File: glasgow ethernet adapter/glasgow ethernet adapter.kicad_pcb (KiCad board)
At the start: 2 copper layers, 33 parts, among them J1 Glasgow Port, J2 RJ45_Amphenol_RJMG1BD3B8K1ANR, U1 MxL86110

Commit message: WIP
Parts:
- added C17: 4.7u, Capacitor_SMD:C_1206_3216Metric, F.Cu at (178.2, 121.3)
- added C18: 0.1u, Capacitor_SMD:C_0402_1005Metric, F.Cu at (198.8, 100.2)
- added C19: 0.1u, Capacitor_SMD:C_0402_1005Metric, F.Cu at (162.1, 95.9)
- added C20: 4.7u, Capacitor_SMD:C_1206_3216Metric, F.Cu at (150.0, 82.5)
- added C21: 0.1u, Capacitor_SMD:C_0402_1005Metric, F.Cu at (198.9, 101.7)
- added C22: 0.1u, Capacitor_SMD:C_0402_1005Metric, F.Cu at (139.6, 110.4)
- added D1: LED, Diode_SMD:D_0603_1608Metric, F.Cu at (135.7, 87.3)
- added D2: LED, Diode_SMD:D_0603_1608Metric, F.Cu at (135.7, 84.2)
- added D3: LED, Diode_SMD:D_0603_1608Metric, F.Cu at (135.7, 81.1)
- added R14: 49.9, Resistor_SMD:R_0402_1005Metric, F.Cu at (155.4, 98.9)
- added R15: 49.9, Resistor_SMD:R_0402_1005Metric, F.Cu at (155.4, 101.7)
- added R16: 49.9, Resistor_SMD:R_0402_1005Metric, F.Cu at (155.4, 103.6)
- added R17: R, Resistor_SMD:R_0402_1005Metric, F.Cu at (138.1, 87.3)
- added R18: R, Resistor_SMD:R_0402_1005Metric, F.Cu at (138.1, 84.2)
- added R19: R, Resistor_SMD:R_0402_1005Metric, F.Cu at (138.1, 81.1)
- C1, C2: value C -> 12p; footprint Capacitor_SMD:C_0603_1608Metric -> Capacitor_SMD:C_0402_1005Metric
- C10, C3, C4, C5, C6, C7, C8, C9: value C -> 0.1u; footprint Capacitor_SMD:C_0603_1608Metric -> Capacitor_SMD:C_0402_1005Metric
- J2: value RJ45_Amphenol_RJMG1BD3B8K1ANR -> RJ45_Amphenol_RJMG1S8008101BR; footprint Connector_RJ:RJ45_Amphenol_RJMG1BD3B8K1ANR -> glasgow:AMPHENOL_RJMG1S8008101BR
- R1, R2, R3, R4, R6, R7, R8, R9: value R -> R-3-way; footprint Resistor_SMD:R_0603_1608Metric -> glasgow:R-3-Way_0402_1005Metric
- R10: value 49.9 -> 0; footprint Resistor_SMD:R_0603_1608Metric -> Resistor_SMD:R_0402_1005Metric
- R11: value 49.9 -> R; footprint Resistor_SMD:R_0603_1608Metric -> Resistor_SMD:R_0402_1005Metric
- R12: value 49.9 -> 2.49K; footprint Resistor_SMD:R_0603_1608Metric -> Resistor_SMD:R_0402_1005Metric
- R13: footprint Resistor_SMD:R_0603_1608Metric -> Resistor_SMD:R_0402_1005Metric
- R5: value 2.49K -> R-3-way; footprint Resistor_SMD:R_0603_1608Metric -> glasgow:R-3-Way_0402_1005Metric
- U1: footprint Package_DFN_QFN:QFN-40-1EP_5x5mm_P0.4mm_EP3.8x3.8mm -> glasgow:QFN-40-1EP_5x5mm_P0.4mm_EP3.8x3.8mm
- moved R6 61.7 mm to (153.4, 89.4), turned to 90 degrees
- moved C14 59.9 mm to (153.4, 104.2)
- moved R3 59.8 mm to (155.1, 88.8), turned to 90 degrees
- moved C13 59.7 mm to (153.4, 101.2)
- moved C16 58.4 mm to (153.4, 102.7), turned to 180 degrees
- moved C15 58.1 mm to (153.4, 98.0), turned to 180 degrees
- moved C12 53.6 mm to (153.4, 99.5)
- moved C11 53.5 mm to (153.4, 96.5)
- moved C9 49.7 mm to (158.8, 102.9), turned to -90 degrees
- moved C7 49.7 mm to (158.9, 97.8), turned to 90 degrees
- moved R2 47.0 mm to (171.1, 101.9), turned to 90 degrees
- moved L1 45.1 mm to (165.8, 95.3), turned to 90 degrees
- moved C3 44.9 mm to (160.3, 104.2), turned to -90 degrees
- moved C5 43.2 mm to (159.7, 96.4), turned to 180 degrees
- moved C8 43.2 mm to (166.3, 102.5), turned to -90 degrees
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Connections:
- net Net-(U1-REG_O) renamed +1V1
- C11 pad 1: Net-(J2-TD+) -> /T+
- C11 pad 2: Net-(U1-TRXN1) -> /TX+
- C12 pad 1: Net-(J2-TD-) -> /T-
- C12 pad 2: Net-(U1-TRXP1) -> /TX-
- C13 pad 1: Net-(J2-RD+) -> /R+
- C13 pad 2: Net-(U1-TRXN0) -> /RX+
- C14 pad 1: Net-(J2-RD-) -> /R-
- C14 pad 2: Net-(U1-TRXP0) -> /RX-
- J1 pad A0: /G_RX_CLK -> /GPC
- J1 pad A1: /PHYAD2 -> /MDINT
- J1 pad A2: /RXD0 -> /PHYAD1
- J1 pad A3: /RXD1 -> /PHYAD2
- J1 pad A4: /PLLOFF -> /RXD0
- J1 pad A5: /PHYAD0 -> /RXD1
- J1 pad A6: /MDINT -> /PLLOFF
- J1 pad A7: unconnected-(J1-PadA7) -> /PHYAD0
- J1 pad B0: /G_TX_CLK -> /TX_CLK
- J1 pad B7: /GPC -> unconnected-(J1-PadB7)
- J2 pad SH: unconnected-(J2-PadSH) -> C_GND
- R1 pad 1: /G_TX_CLK -> GND
- R1 pad 2: /TX_CLK -> /PLLOFF
- R10 pad 1: Net-(U1-TRXN1) -> C_GND
- R10 pad 2: Net-(J2-TCT) -> GND
- R11 pad 1: Net-(J2-TCT) -> +3V3
- R11 pad 2: Net-(U1-TRXP1) -> Net-(U1-RSTN)
- R12 pad 1: Net-(U1-TRXN0) -> GND
- R12 pad 2: Net-(J2-RCT) -> Net-(U1-RBIAS)
- R13 pad 1: Net-(J2-RCT) -> /TX+
- R13 pad 2: Net-(U1-TRXP0) -> Net-(J2-TCT)
- R2 pad 1: GND -> +3V3
- R2 pad 2: /CFG_LDO0 -> /PHYAD0
- R3 pad 2: /CFG_LDO1 -> /CFG_LDO0
- R4 pad 2: Net-(U1-RSTN) -> /RXD1
- R5 pad 1: GND -> +3V3
- R5 pad 2: Net-(U1-RBIAS) -> /PHYAD1
- R6 pad 1: /CFG_EXT -> GND
- R6 pad 2: +3V3 -> /CFG_LDO1
- R7 pad 1: GND -> +3V3
- R7 pad 2: /PLLOFF -> /RXD0
- R8 pad 2: /RXD1 -> /PHYAD2
- R9 pad 2: /RXD0 -> /CFG_EXT
- U1 pad 1: Net-(U1-TRXP0) -> unconnected-(U1-TRXP0-Pad1)
- U1 pad 2: Net-(U1-TRXN0) -> unconnected-(U1-TRXN0-Pad2)
- U1 pad 4: Net-(U1-TRXP1) -> /TX+
- U1 pad 5: Net-(U1-TRXN1) -> /TX-
- U1 pad 6: unconnected-(U1-TRXP2-Pad6) -> /RX+
- U1 pad 7: unconnected-(U1-TRXN2-Pad7) -> /RX-
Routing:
- net +3V3: track 0.00 -> 245.2 mm, vias 0 -> 5
- net /AVDDL: track 0.00 -> 56.9 mm, vias 0 -> 10
- net GND: track 0.00 -> 42.4 mm, vias 0 -> 31
- net /CFG_LDO1: track 0.00 -> 41.8 mm, vias 0 -> 2
- net /CFG_EXT: track 0.00 -> 41.1 mm, vias 0 -> 2
- net /CFG_LDO0: track 0.00 -> 40.5 mm, vias 0 -> 2
- net /PHYAD1: track 0.00 -> 28.2 mm
- net /PHYAD0: track 0.00 -> 27.5 mm
- net /PHYAD2: track 0.00 -> 26.7 mm
- net /RXD1: track 2.96 -> 29.1 mm
- net /RXD0: track 3.05 -> 27.7 mm
- net /PLLOFF: track 3.01 -> 27.5 mm
- net /GPC: track 0.00 -> 19.2 mm
- net /TX_CLK: track 0.00 -> 18.9 mm
- net /MDINT: track 0.00 -> 18.5 mm
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- added copper zone on B.Cu, net C_GND
- added copper zone on B.Cu, net GND
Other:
- board outline added: 61.7 x 49 mm

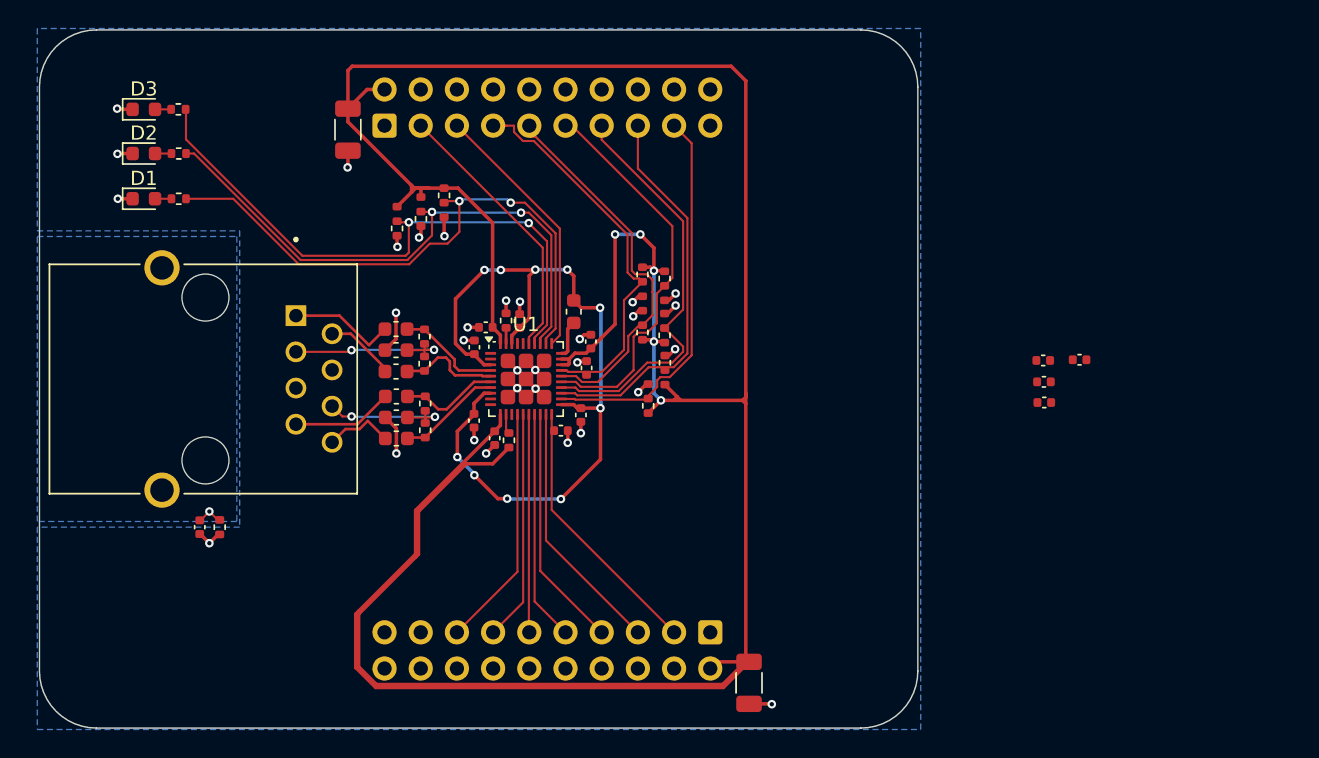
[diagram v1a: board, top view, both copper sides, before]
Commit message: wip - connect MDC, add crystal
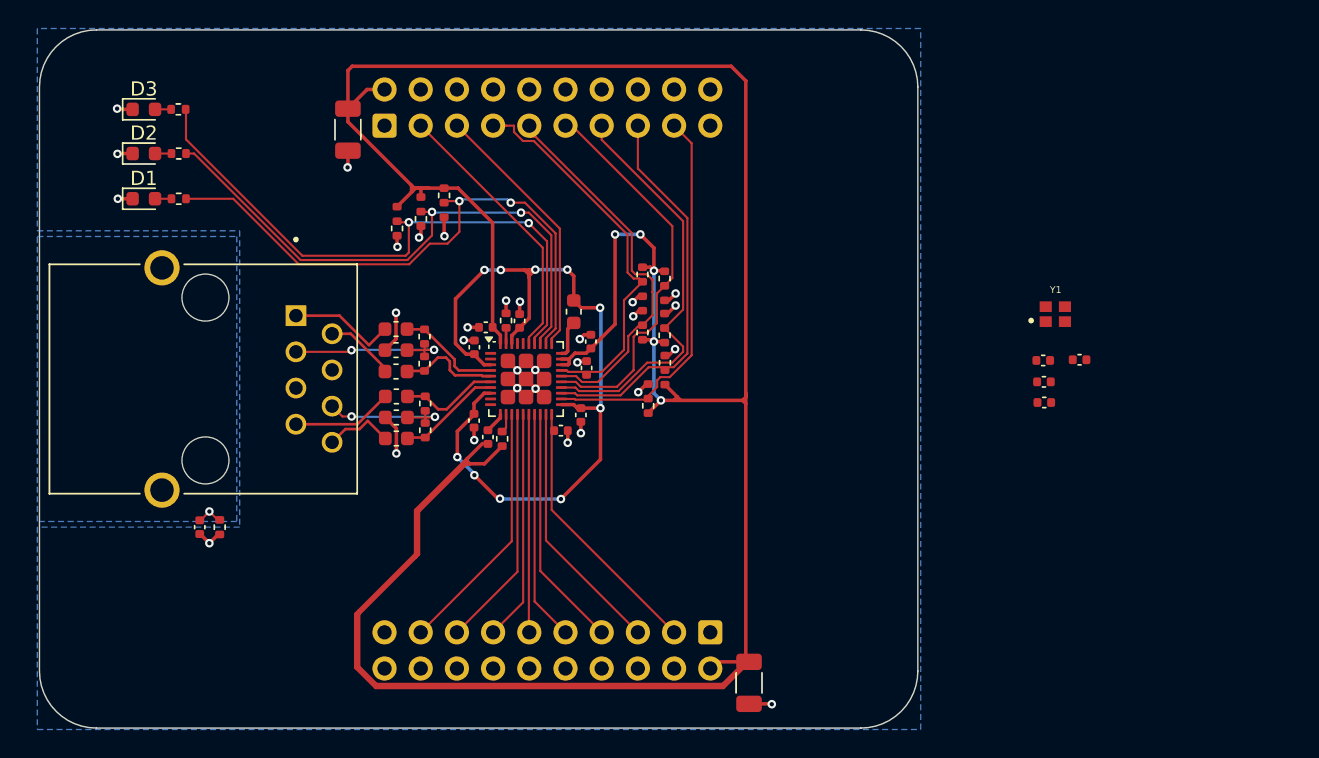
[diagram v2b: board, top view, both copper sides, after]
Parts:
- added Y1: 25 MHz, glasgow:XTAL_ECS-160-9-37-CKM-TR, F.Cu at (199.7, 95.5)
- moved R11 0.49 mm to (160.8, 104.2)
- moved C3 0.48 mm to (159.8, 104.1)
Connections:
- J1 pad B7: unconnected-(J1-PadB7) -> /MDC
- U1 pad 13: unconnected-(U1-MDC-Pad13) -> /MDC
- U1 pad 36: unconnected-(U1-XTAL_I-Pad36) -> /XTAL_I
- U1 pad 37: unconnected-(U1-XTAL_O-Pad37) -> /XTAL_O
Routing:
- net /MDC: track 0.00 -> 17.9 mm
- net /AVDDL: track 56.9 -> 58.0 mm
- net +3V3: track 245.2 -> 244.3 mm
- net GND: track 42.4 -> 41.5 mm, vias 31 -> 30

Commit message: wip - add 4-pair RJ45, switch to 4 layers
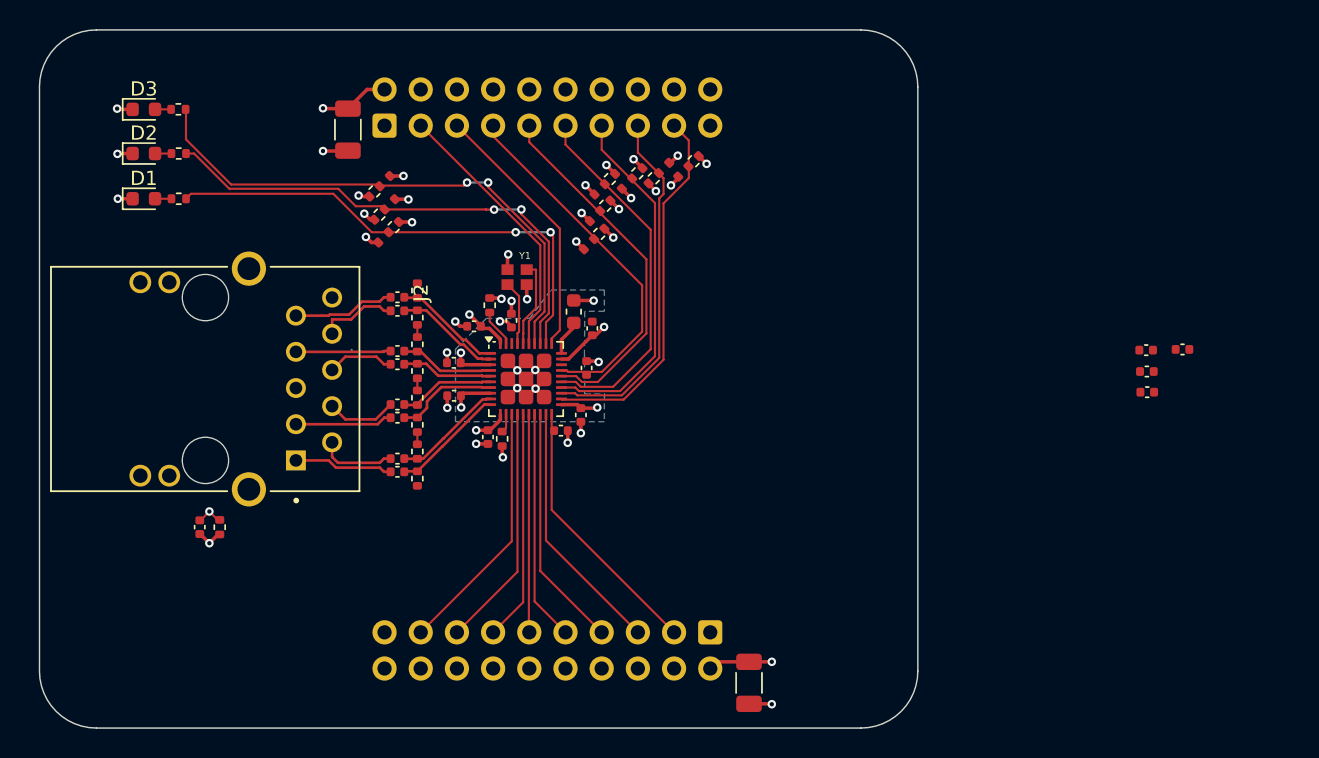
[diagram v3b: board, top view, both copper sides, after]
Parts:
- added C23: 6.8 nF, Capacitor_SMD:C_0402_1005Metric, F.Cu at (153.5, 105.6)
- added C24: 6.8 nF, Capacitor_SMD:C_0402_1005Metric, F.Cu at (153.5, 106.5)
- added R20: 49.9, Resistor_SMD:R_0402_1005Metric, F.Cu at (154.9, 101.3)
- added R21: 49.9, Resistor_SMD:R_0402_1005Metric, F.Cu at (154.9, 103.2)
- added R22: 49.9, Resistor_SMD:R_0402_1005Metric, F.Cu at (154.9, 105.1)
- added R23: 49.9, Resistor_SMD:R_0402_1005Metric, F.Cu at (154.9, 107.0)
- C11, C12, C13, C14: footprint Capacitor_SMD:C_0603_1608Metric -> Capacitor_SMD:C_0402_1005Metric
- C15, C16: value .01 uF -> 6.8 nF; footprint Capacitor_SMD:C_0603_1608Metric -> Capacitor_SMD:C_0402_1005Metric
- J2: value RJ45_Amphenol_RJMG1S8008101BR -> RJ45_Amphenol_RJMG201K21120FR; footprint glasgow:AMPHENOL_RJMG1S8008101BR -> glasgow:AMPHENOL_RJMG201K21120FR
- moved Y1 37.9 mm to (161.9, 92.8), turned to 180 degrees
- moved R2 17.5 mm to (174.3, 84.7), turned to -135 degrees
- moved R1 13.0 mm to (171.5, 85.9), turned to 45 degrees
- moved R4 11.5 mm to (170.3, 85.6), turned to -135 degrees
- moved R8 9.27 mm to (168.1, 87.8), turned to -135 degrees
- moved R7 7.97 mm to (168.4, 86.0), turned to -135 degrees
- moved C10 7.26 mm to (208.6, 97.9)
- moved C18 7.26 mm to (206.1, 99.5)
- moved C21 7.26 mm to (206.1, 100.9)
- moved C6 7.26 mm to (206.0, 98.0)
- moved C14 5.21 mm to (153.5, 99.0)
- moved C12 4.26 mm to (153.5, 95.2)
- moved R15 4.20 mm to (154.9, 97.6), turned to 90 degrees
- moved R16 4.20 mm to (154.9, 99.4), turned to 90 degrees
- moved R9 4.18 mm to (153.2, 89.3), turned to -135 degrees
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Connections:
- net /R+ renamed /TDX2+
- net /R- renamed /TDX2-
- C11 pad 1: /T+ -> /TDX1+
- C11 pad 2: /TX+ -> /TRX1+
- C12 pad 1: /T- -> /TDX1-
- C12 pad 2: /TX- -> /TRX1-
- C13 pad 2: /RX+ -> /TRX2+
- C14 pad 2: /RX- -> /TRX2-
- C15 pad 1: Net-(J2-TCT) -> /TDX3+
- C15 pad 2: GND -> /TRX3+
- C16 pad 1: Net-(J2-RCT) -> /TDX3-
- C16 pad 2: GND -> /TRX3-
- J2 pad 1: /T+ -> GND
- J2 pad 2: /T- -> /TDX4+
- J2 pad 3: Net-(J2-TCT) -> /TDX4-
- J2 pad 4: (no net) -> /TDX3+
- J2 pad 5: (no net) -> /TDX3-
- J2 pad 6: Net-(J2-RCT) -> /TCT
- R13 pad 1: /TX+ -> /TRX1+
- R13 pad 2: Net-(J2-TCT) -> /TCT
- R14 pad 1: Net-(J2-TCT) -> /TCT
- R14 pad 2: /TX- -> /TRX1-
- R15 pad 1: /RX+ -> /TRX2+
- R15 pad 2: Net-(J2-RCT) -> /TCT
- R16 pad 1: Net-(J2-RCT) -> /TCT
- R16 pad 2: /RX- -> /TRX2-
- U1 pad 1: unconnected-(U1-TRXP0-Pad1) -> /TRX1+
- U1 pad 10: unconnected-(U1-TRXN3-Pad10) -> /TRX4-
- U1 pad 2: unconnected-(U1-TRXN0-Pad2) -> /TRX1-
- U1 pad 4: /TX+ -> /TRX2+
- U1 pad 5: /TX- -> /TRX2-
- U1 pad 6: /RX+ -> /TRX3+
- U1 pad 7: /RX- -> /TRX3-
- U1 pad 9: unconnected-(U1-TRXP3-Pad9) -> /TRX4+
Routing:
- net +3V3: track 244.3 -> 28.4 mm, vias 5 -> 15
- net /AVDDL: track 58.0 -> 11.0 mm, vias 10 -> 5
- net Net-(J2-TCT): track 12.5 -> 0.00 mm, vias 2 -> 0
- net Net-(J2-RCT): track 10.4 -> 0.00 mm, vias 2 -> 0
- net /TRX4-: track 0.00 -> 8.05 mm
- net /TRX4+: track 0.00 -> 7.80 mm
- net /TRX1-: track 0.00 -> 7.78 mm
- net /TRX1+: track 0.00 -> 7.69 mm
- net /T+: track 7.57 -> 0.00 mm
- net /TX+: track 7.34 -> 0.00 mm
- net /RX-: track 7.32 -> 0.00 mm
- net /TRX3-: track 0.00 -> 7.23 mm
- net /TDX1+: track 0.00 -> 7.18 mm
- net /TX-: track 7.16 -> 0.00 mm
- net /RX+: track 7.02 -> 0.00 mm
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- added copper zone on In2.Cu, net +3V3
- added copper zone on B.Cu, net /AVDDL
- added copper zone on In1.Cu, net C_GND
- added copper zone on In1.Cu, net GND
- removed copper zone on B.Cu, net C_GND
- removed copper zone on B.Cu, net GND
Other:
- copper layers 2 -> 4

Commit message: wip - add silkscreen
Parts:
- added REF**: cat, glasgow:cat, F.Cu at (180.2, 99.7)
- moved C6 38.2 mm to (167.8, 97.8)
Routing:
- net /TCT: track 2.57 -> 26.9 mm, vias 0 -> 5
- net +3V3: track 28.4 -> 37.1 mm, vias 15 -> 16
- net /TDX2-: track 4.71 -> 8.80 mm
- net /TDX3+: track 4.92 -> 8.07 mm
- net /TDX1-: track 5.61 -> 8.42 mm
- net /TDX2+: track 6.67 -> 9.48 mm
- net +1V1: track 2.49 -> 0.00 mm
- net /TDX4+: track 5.42 -> 7.73 mm
- net GND: track 37.9 -> 40.1 mm, vias 30 -> 31
- net /TDX3-: track 6.84 -> 8.59 mm
- net /TDX1+: track 7.18 -> 8.93 mm
- net /TDX4-: track 6.98 -> 8.48 mm
- net /AVDDL: track 11.0 -> 12.1 mm
- added copper zone on F.Cu, net +1V1
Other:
- board text added: "0"
- board text added: "1"
- board text added: "2"
- board text added: "25 MHz"
- board text added: "3"
- board text added: "GPC"
- board text added: "LED0"
- board text added: "LED1"
- board text added: "LED2"
- board text added: "MDC"
- board text added: "MDINT"
- board text added: "MDIO"
- board text added: "RST"
- board text added: "RX CLK"
- board text added: "RX CTL"
- board text added: "RXD0:3"
- board text added: "TX CLK"
- board text added: "TX CTL"
- board text added: "TXD3:0"

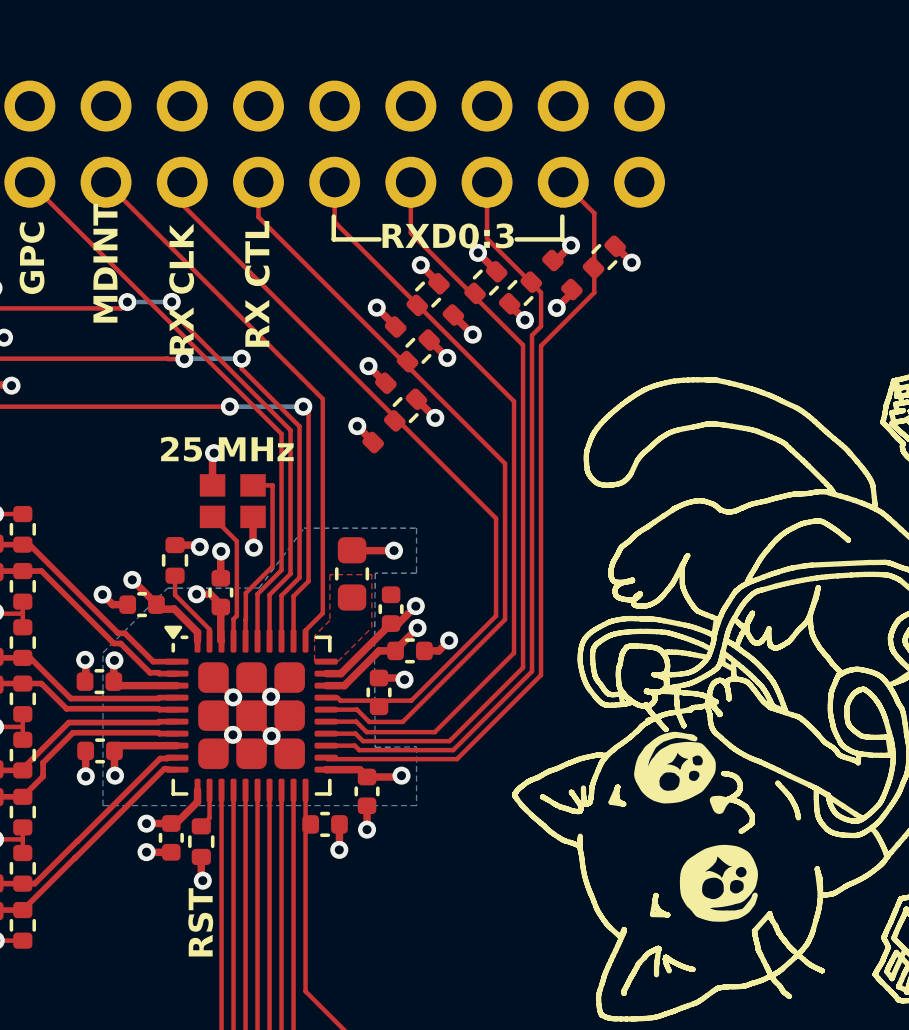
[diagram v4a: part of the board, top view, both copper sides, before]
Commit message: move strap resistors closer to PHY
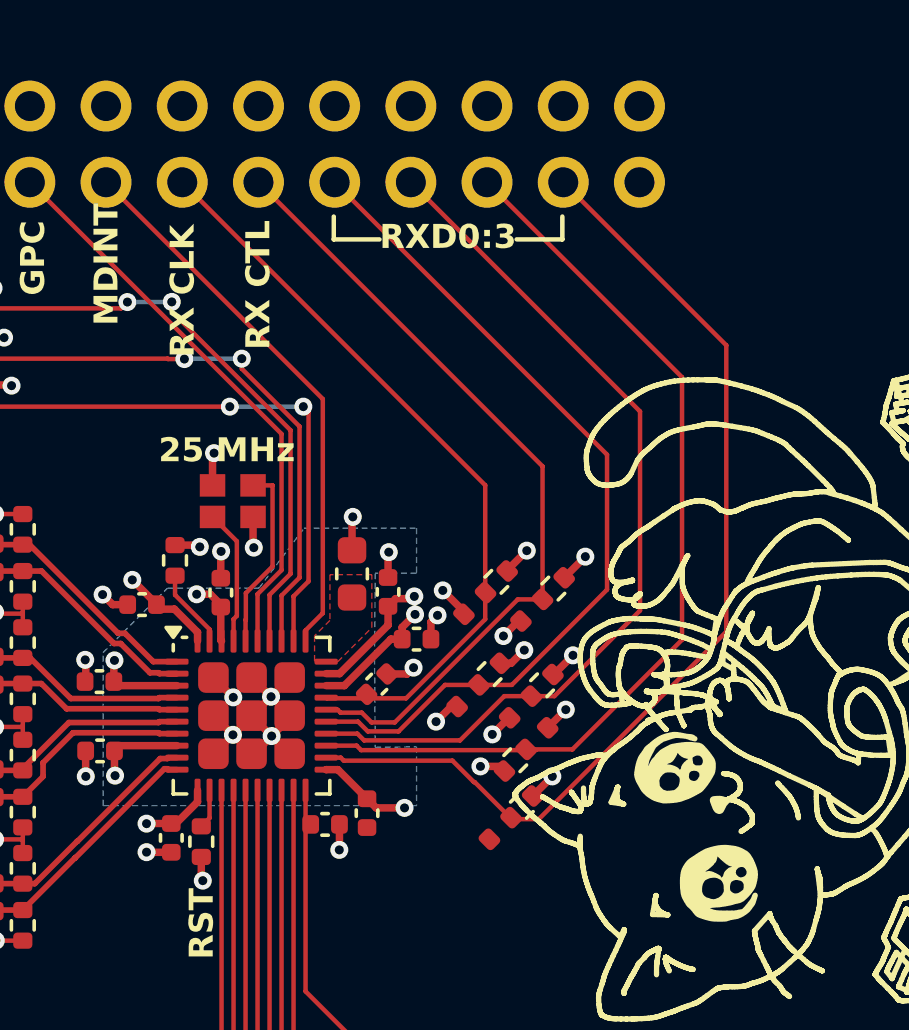
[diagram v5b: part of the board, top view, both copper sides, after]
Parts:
- moved R2 18.5 mm to (171.5, 103.0)
- moved R1 15.6 mm to (171.3, 101.5)
- moved R4 13.6 mm to (172.2, 99.0)
- moved R7 12.8 mm to (170.4, 98.6)
- moved R8 9.11 mm to (172.6, 95.8)
- moved R5 6.48 mm to (170.7, 95.5)
- moved C8 0.72 mm to (166.3, 103.2)
- moved C4 0.58 mm to (167.1, 95.9)
- moved C6 0.45 mm to (168.0, 97.5)
- moved C2 0.29 mm to (166.7, 99.0), turned to 45 degrees
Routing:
- net /PHYAD0: track 25.9 -> 34.0 mm
- net /PLLOFF: track 25.2 -> 31.7 mm
- net /RXD1: track 25.4 -> 29.8 mm
- net /RXD0: track 25.7 -> 28.8 mm
- net +3V3: track 37.1 -> 38.4 mm
- net /PHYAD2: track 25.5 -> 26.8 mm
- net GND: track 40.1 -> 39.5 mm, vias 31 -> 30
- net /PHYAD1: track 25.7 -> 25.2 mm
